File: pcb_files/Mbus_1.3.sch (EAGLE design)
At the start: 48 parts, among them IC1 NCP1117ST50T3G, IC3 ATMEGA2560-16AU, IC4 RTC_PCF8523T, J1 F-1X18-SIP-100-32Y, J2 USB_A_SMT_FEMALE, M1 SERVO, Q1 BSS138, Q2 32.768, Q3 BSS138, Y1 CSTCE16M0V53-R0 16MHZ

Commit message: Trial on polygon
Signed-off-by: Yiteng Cai <alonsochate@umich.edu>
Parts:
- added R16: 10k, SmartPrj:R-EU_R0603
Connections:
- removed net PISCL: IC4.SCL, PIHEADER.SCL/GP3\, R5.2
- removed net PISDA: IC4.SDA, PIHEADER.SDA/GP2, R6.1
- net +3V3: now also PIHEADER.3.3V, R16.2, R7.1, SJ3.2, SJ4.2
- net +5V: no longer PIHEADER.5V, R7.1, SJ3.2, SJ4.2
- net PD7: now also PIHEADER.SCL/GP3\, R16.1
- net RXD3: now also IC3.PJ0(RXD3/PCINT9)
- net SCL: now also IC4.SCL, R5.2
- net SDA: now also IC4.SDA, R6.1
- net TXD3: now also IC3.PJ1(TXD3/PCINT10)
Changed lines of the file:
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@@
 <part name="P+20" library="supply1@1" deviceset="+5V" device=""/>
 <part name="R8" library="rcl@1" deviceset="POTENTIOMETER_" device="PT-10"/>
-<part name="P+6" library="supply1@1" deviceset="+5V" device=""/>
 <part name="TESTPIN" library="SmartPrj" deviceset="PINHD-1X8" device="" value="8x1F-H8.5"/>
-<part name="P+2" library="supply1@1" deviceset="+5V" device=""/>
-<part name="P+12" library="supply1@1" deviceset="+5V" device=""/>
 <part name="J1" library="con-headers-jp" deviceset="F-1X18-" device="SIP-100-32Y"/>
 <part name="P+18" library="supply1@1" deviceset="+5V" device=""/>
@@
 <part name="R14" library="SmartPrj" deviceset="R-EU_" device="R0603" value="10k"/>
 <part name="R15" library="SmartPrj" deviceset="R-EU_" device="R0603" value="10k"/>
+<part name="+3V5" library="supply1" deviceset="+3V3" device=""/>
+<part name="+3V6" library="supply1" deviceset="+3V3" device=""/>
+<part name="+3V7" library="supply1" deviceset="+3V3" device=""/>
+<part name="+3V8" library="supply1" deviceset="+3V3" device=""/>
+<part name="R16" library="SmartPrj" deviceset="R-EU_" device="R0603" value="10k"/>
 </parts>
 <sheets>
@@
 <attribute name="VALUE" x="210.82" y="88.9" size="1.778" layer="96"/>
 </instance>
-<instance part="P+6" gate="1" x="264.16" y="134.62" smashed="yes">
-<attribute name="VALUE" x="261.62" y="129.54" size="1.778" layer="96" rot="R90"/>
-</instance>
 <instance part="TESTPIN" gate="A" x="68.58" y="10.16" smashed="yes">
 <attribute name="NAME" x="72.39" y="10.795" size="1.778" layer="95"/>
 <attribute name="VALUE" x="62.23" y="-2.54" size="1.778" layer="96"/>
 </instance>
-<instance part="P+2" gate="1" x="297.18" y="50.8" smashed="yes">
-<attribute name="VALUE" x="294.64" y="45.72" size="1.778" layer="96" rot="R90"/>
-</instance>
-<instance part="P+12" gate="1" x="271.78" y="33.02" smashed="yes">
-<attribute name="VALUE" x="269.24" y="27.94" size="1.778" layer="96" rot="R90"/>
-</instance>
 <instance part="J1" gate="G$1" x="218.44" y="-7.62" smashed="yes">
 <attribute name="VALUE" x="217.17" y="-35.56" size="1.778" layer="96"/>
@@
 <attribute name="NAME" x="328.5236" y="76.2" size="1.778" layer="95" rot="R270"/>
 <attribute name="VALUE" x="328.168" y="69.215" size="1.778" layer="96" rot="R270"/>
+</instance>
+<instance part="+3V5" gate="G$1" x="254" y="127" smashed="yes">
+<attribute name="VALUE" x="251.46" y="121.92" size="1.778" layer="96" rot="R90"/>
+</instance>
+<instance part="+3V6" gate="G$1" x="297.18" y="50.8" smashed="yes">
+<attribute name="VALUE" x="294.64" y="45.72" size="1.778" layer="96" rot="R90"/>
+</instance>
+<instance part="+3V7" gate="G$1" x="271.78" y="40.64" smashed="yes">
+<attribute name="VALUE" x="269.24" y="35.56" size="1.778" layer="96" rot="R90"/>
+</instance>
+<instance part="+3V8" gate="G$1" x="317.5" y="142.24" smashed="yes">
+<attribute name="VALUE" x="314.96" y="137.16" size="1.778" layer="96" rot="R90"/>
+</instance>
+<instance part="R16" gate="G$1" x="317.5" y="132.08" smashed="yes" rot="R90">
+<attribute name="NAME" x="313.2836" y="134.62" size="1.778" layer="95" rot="R270"/>
+<attribute name="VALUE" x="312.928" y="127.635" size="1.778" layer="96" rot="R270"/>
 </instance>
 </instances>
@@
 <wire x1="223.52" y1="96.52" x2="213.36" y2="96.52" width="0.1524" layer="91"/>
 <junction x="223.52" y="96.52"/>
-</segment>
-<segment>
-<pinref part="P+6" gate="1" pin="+5V"/>
-<wire x1="264.16" y1="132.08" x2="264.16" y2="129.54" width="0.1524" layer="91"/>
-<pinref part="PIHEADER" gate="G$1" pin="5V"/>
-<wire x1="264.16" y1="129.54" x2="271.78" y2="129.54" width="0.1524" layer="91"/>
-</segment>
-<segment>
-<pinref part="R7" gate="G$1" pin="1"/>
-<wire x1="297.18" y1="48.26" x2="297.18" y2="43.18" width="0.1524" layer="91"/>
-<pinref part="P+2" gate="1" pin="+5V"/>
-</segment>
-<segment>
-<pinref part="SJ3" gate="G$1" pin="2"/>
-<pinref part="SJ4" gate="G$1" pin="2"/>
-<wire x1="274.32" y1="30.48" x2="271.78" y2="30.48" width="0.1524" layer="91"/>
-<pinref part="P+12" gate="1" pin="+5V"/>
-<wire x1="271.78" y1="30.48" x2="266.7" y2="30.48" width="0.1524" layer="91"/>
-<junction x="271.78" y="30.48"/>
 </segment>
 <segment>
@@
 <label x="58.42" y="17.78" size="1.778" layer="95"/>
 </segment>
+<segment>
+<wire x1="287.02" y1="2.54" x2="266.7" y2="2.54" width="0.1524" layer="91"/>
+<wire x1="266.7" y1="2.54" x2="266.7" y2="5.08" width="0.1524" layer="91"/>
+<label x="274.32" y="2.54" size="1.778" layer="95"/>
+<pinref part="R6" gate="G$1" pin="1"/>
+<pinref part="IC4" gate="G$1" pin="SDA"/>
+</segment>
 </net>
 <net name="SCL" class="0">
@@
 <wire x1="66.04" y1="20.32" x2="55.88" y2="20.32" width="0.1524" layer="91"/>
 <label x="58.42" y="20.32" size="1.778" layer="95"/>
+</segment>
+<segment>
+<wire x1="287.02" y1="5.08" x2="274.32" y2="5.08" width="0.1524" layer="91"/>
+<label x="279.4" y="5.08" size="1.778" layer="95"/>
+<pinref part="R5" gate="G$1" pin="2"/>
+<pinref part="IC4" gate="G$1" pin="SCL"/>
 </segment>
 </net>
@@
 </segment>
 </net>
-<net name="PISDA" class="0">
-<segment>
-<pinref part="PIHEADER" gate="G$1" pin="SDA/GP2"/>
-<wire x1="302.26" y1="124.46" x2="309.88" y2="124.46" width="0.1524" layer="91"/>
-<label x="307.34" y="124.46" size="1.778" layer="95"/>
-</segment>
-<segment>
-<wire x1="287.02" y1="2.54" x2="266.7" y2="2.54" width="0.1524" layer="91"/>
-<wire x1="266.7" y1="2.54" x2="266.7" y2="5.08" width="0.1524" layer="91"/>
-<label x="274.32" y="2.54" size="1.778" layer="95"/>
-<pinref part="R6" gate="G$1" pin="1"/>
-<pinref part="IC4" gate="G$1" pin="SDA"/>
-</segment>
-</net>
-<net name="PISCL" class="0">
-<segment>
-<pinref part="PIHEADER" gate="G$1" pin="SCL/GP3\"/>
-<wire x1="302.26" y1="121.92" x2="309.88" y2="121.92" width="0.1524" layer="91"/>
-<label x="307.34" y="121.92" size="1.778" layer="95"/>
-</segment>
-<segment>
-<wire x1="287.02" y1="5.08" x2="274.32" y2="5.08" width="0.1524" layer="91"/>
-<label x="279.4" y="5.08" size="1.778" layer="95"/>
-<pinref part="R5" gate="G$1" pin="2"/>
-<pinref part="IC4" gate="G$1" pin="SCL"/>
-</segment>
-</net>
 <net name="N$11" class="0">
 <segment>
@@
 <pinref part="J1" gate="G$1" pin="6"/>
 </segment>
+<segment>
+<pinref part="IC3" gate="1" pin="PJ1(TXD3/PCINT10)"/>
+<wire x1="104.14" y1="12.7" x2="91.44" y2="12.7" width="0.1524" layer="91"/>
+<label x="88.9" y="15.24" size="1.778" layer="95"/>
+</segment>
 </net>
 <net name="RXD3" class="0">
@@
 <pinref part="J1" gate="G$1" pin="7"/>
 </segment>
+<segment>
+<pinref part="IC3" gate="1" pin="PJ0(RXD3/PCINT9)"/>
+<wire x1="104.14" y1="10.16" x2="91.44" y2="10.16" width="0.1524" layer="91"/>
+<label x="88.9" y="7.62" size="1.778" layer="95"/>
+</segment>
 </net>
 <net name="PD5" class="0">
@@
 <pinref part="J1" gate="G$1" pin="5"/>
 </segment>
+<segment>
+<pinref part="PIHEADER" gate="G$1" pin="SCL/GP3\"/>
+<pinref part="R16" gate="G$1" pin="1"/>
+<wire x1="302.26" y1="121.92" x2="317.5" y2="121.92" width="0.1524" layer="91"/>
+<wire x1="317.5" y1="121.92" x2="317.5" y2="127" width="0.1524" layer="91"/>
+<wire x1="317.5" y1="121.92" x2="325.12" y2="121.92" width="0.1524" layer="91"/>
+<junction x="317.5" y="121.92"/>
+<label x="325.12" y="121.92" size="1.778" layer="95"/>
+</segment>
 </net>
 <net name="+3V3" class="0">
@@
 <wire x1="332.74" y1="81.28" x2="332.74" y2="78.74" width="0.1524" layer="91"/>
 </segment>
-</net>
+<segment>
+<pinref part="+3V5" gate="G$1" pin="+3V3"/>
+<pinref part="PIHEADER" gate="G$1" pin="3.3V"/>
+<wire x1="254" y1="124.46" x2="271.78" y2="124.46" width="0.1524" layer="91"/>
+<wire x1="271.78" y1="124.46" x2="271.78" y2="127" width="0.1524" layer="91"/>
+</segment>
+<segment>
+<pinref part="R7" gate="G$1" pin="1"/>
+<wire x1="297.18" y1="48.26" x2="297.18" y2="43.18" width="0.1524" layer="91"/>
+<pinref part="+3V6" gate="G$1" pin="+3V3"/>
+</segment>
+<segment>
+<pinref part="SJ3" gate="G$1" pin="2"/>
+<pinref part="SJ4" gate="G$1" pin="2"/>
+<wire x1="274.32" y1="30.48" x2="271.78" y2="30.48" width="0.1524" layer="91"/>
+<pinref part="+3V7" gate="G$1" pin="+3V3"/>
+<wire x1="271.78" y1="30.48" x2="266.7" y2="30.48" width="0.1524" layer="91"/>
+<wire x1="271.78" y1="38.1" x2="271.78" y2="30.48" width="0.1524" layer="91"/>
+<junction x="271.78" y="30.48"/>
+</segment>
+<segment>
+<pinref part="R16" gate="G$1" pin="2"/>
+<pinref part="+3V8" gate="G$1" pin="+3V3"/>
+<wire x1="317.5" y1="137.16" x2="317.5" y2="139.7" width="0.1524" layer="91"/>
+</segment>
+</net>

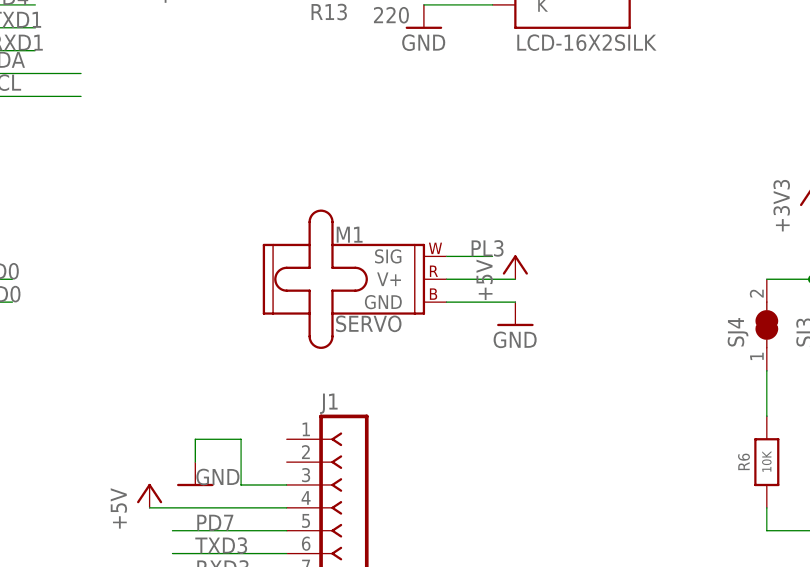
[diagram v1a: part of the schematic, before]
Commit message: Modify the npn transistor and board layout for 1.2
Signed-off-by: Yiteng Cai <alonsochate@umich.edu>
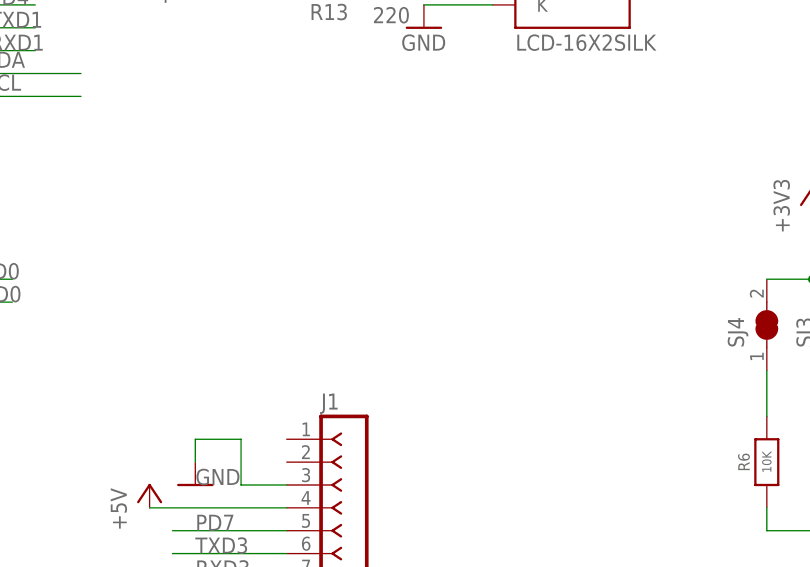
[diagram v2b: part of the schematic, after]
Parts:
- removed M1: SERVO, SparkFun-Electromechanical:SERVO
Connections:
- net +5V: no longer M1.V+
- net GND: no longer M1.GND
- net PL3: no longer M1.SIG
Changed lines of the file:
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@@
 <part name="POWER" library="SmartPrj" deviceset="PINHD-1X8" device="" value="8x1F-H8.5"/>
 <part name="PIHEADER" library="SparkFun-Connectors" deviceset="RASPBERRYPI-40-PIN-GPIO" device="_PTH"/>
-<part name="M1" library="SparkFun-Electromechanical" deviceset="SERVO" device=""/>
-<part name="P+9" library="supply1@1" deviceset="+5V" device=""/>
 <part name="Q2" library="microbuilder" deviceset="CRYSTAL" device="8.0X3.8" value="32.768"/>
 <part name="R5" library="microbuilder" deviceset="RESISTOR" device="0805_NOOUTLINE" value="10K"/>
@@
 <part name="GND22" library="supply1" deviceset="GND" device=""/>
 <part name="GND19" library="supply1@1" deviceset="GND" device=""/>
-<part name="GND26" library="supply1@1" deviceset="GND" device=""/>
 <part name="J2" library="SparkFun-Connectors" deviceset="USB_A" device="_SMT_FEMALE"/>
 <part name="J3" library="SparkFun-Connectors" deviceset="USB_MICRO-B" device="_FEMALE-SMT"/>
@@
 <attribute name="VALUE" x="274.32" y="71.12" size="1.778" layer="96"/>
 </instance>
-<instance part="M1" gate="G$1" x="228.6" y="33.02" smashed="yes">
-<attribute name="NAME" x="218.694" y="34.544" size="1.778" layer="95" font="vector"/>
-<attribute name="VALUE" x="218.694" y="26.416" size="1.778" layer="95" font="vector" align="top-left"/>
-</instance>
-<instance part="P+9" gate="1" x="238.76" y="33.02" smashed="yes">
-<attribute name="VALUE" x="236.22" y="27.94" size="1.778" layer="96" rot="R90"/>
-</instance>
 <instance part="Q2" gate="G$1" x="332.74" y="10.16" smashed="yes" rot="MR270">
 <attribute name="NAME" x="330.2" y="12.7" size="1.27" layer="95" rot="MR270"/>
@@
 <instance part="GND19" gate="1" x="30.48" y="162.56" smashed="yes">
 <attribute name="VALUE" x="27.94" y="160.02" size="1.778" layer="96"/>
-</instance>
-<instance part="GND26" gate="1" x="238.76" y="25.4" smashed="yes">
-<attribute name="VALUE" x="236.22" y="22.86" size="1.778" layer="96"/>
 </instance>
 <instance part="J2" gate="G$1" x="7.62" y="170.18" smashed="yes" rot="MR0">
@@
 </segment>
 <segment>
-<pinref part="M1" gate="G$1" pin="V+"/>
-<wire x1="231.14" y1="30.48" x2="238.76" y2="30.48" width="0.1524" layer="91"/>
-<pinref part="P+9" gate="1" pin="+5V"/>
-</segment>
-<segment>
 <wire x1="213.36" y1="5.08" x2="198.12" y2="5.08" width="0.1524" layer="91"/>
 <pinref part="P+17" gate="1" pin="+5V"/>
@@
 <pinref part="Y1" gate="G$1" pin="2"/>
 <pinref part="GND20" gate="1" pin="GND"/>
-</segment>
-<segment>
-<pinref part="M1" gate="G$1" pin="GND"/>
-<wire x1="231.14" y1="27.94" x2="238.76" y2="27.94" width="0.1524" layer="91"/>
-<pinref part="GND26" gate="1" pin="GND"/>
 </segment>
 <segment>
@@
 <label x="99.06" y="63.5" size="1.778" layer="95"/>
 </segment>
-<segment>
-<pinref part="M1" gate="G$1" pin="SIG"/>
-<wire x1="231.14" y1="33.02" x2="236.22" y2="33.02" width="0.1524" layer="91"/>
-<label x="233.68" y="33.02" size="1.778" layer="95"/>
-</segment>
-</net>
+</net>
